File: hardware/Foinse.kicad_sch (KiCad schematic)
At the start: 81 parts, among them J1 ESQ-110-X-X-D, J15 39-29-1048, J3 PJ-063AH, J4 5023860570, J7 FAULT2, J8 FAULT1, Q1 IPD90P04P4L04ATMA1, Q2 IPD90P04P4L04ATMA1, U1 STM32F072C8Tx, U17 LTC4412xS6, U19 TPS56A37RPAR, U4 TJA1051T-3, U5 TPS563203, U6 ACS71240KEXBLT-010B3, U7 ACS71240KEXBLT-010B3

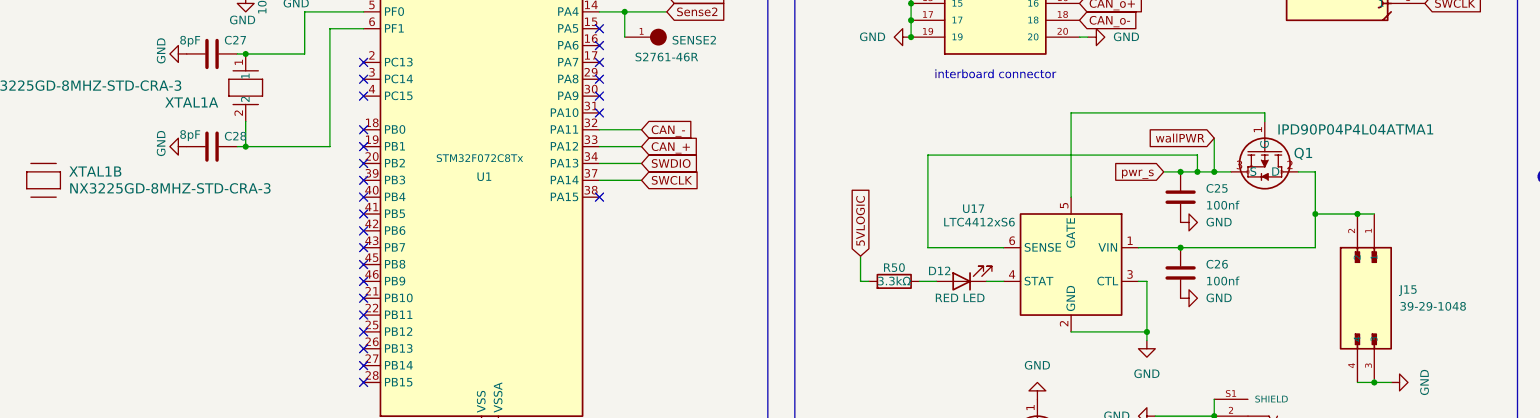
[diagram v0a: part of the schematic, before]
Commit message: added voltage sensing
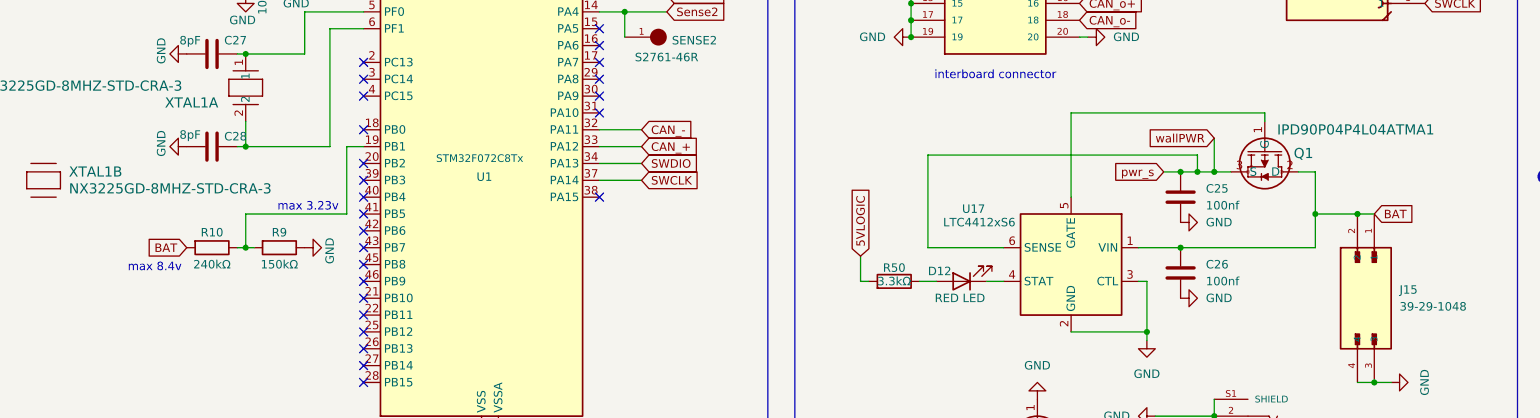
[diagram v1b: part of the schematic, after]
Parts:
- added R10: 240kΩ, Resistor_SMD:R_0402_1005Metric, symbol Device:R
- added R9: 150kΩ, Resistor_SMD:R_0402_1005Metric, symbol Device:R
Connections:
- net GND: now also R9.1
- net BAT: now reaches C26.1, J15.1, J15.2, Q1.2 (D), U17.1 (VIN)
- net BAT: now also R10.2
- net at U1.19 (PB1): now also R10.1, R9.2
- no-connect marks 37 -> 36
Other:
- note added: "max 3.23v"
- note added: "max 8.4v"
